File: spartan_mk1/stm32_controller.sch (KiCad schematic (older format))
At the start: 24 parts, among them SW1 SW_SPST, U4 STM32F405RGTx, Y1 X322516MLB4SI

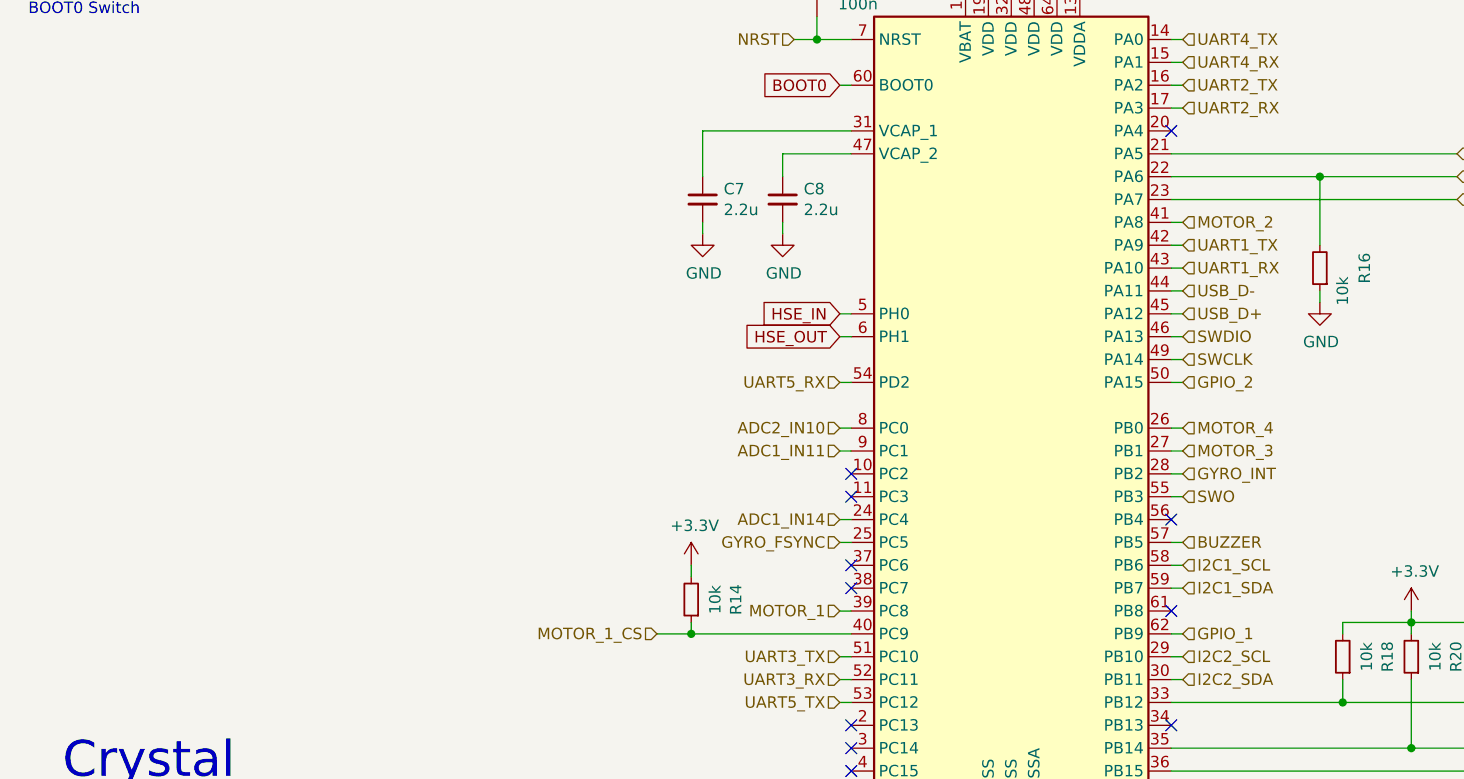
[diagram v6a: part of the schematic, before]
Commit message: Routing complete. Labels complete
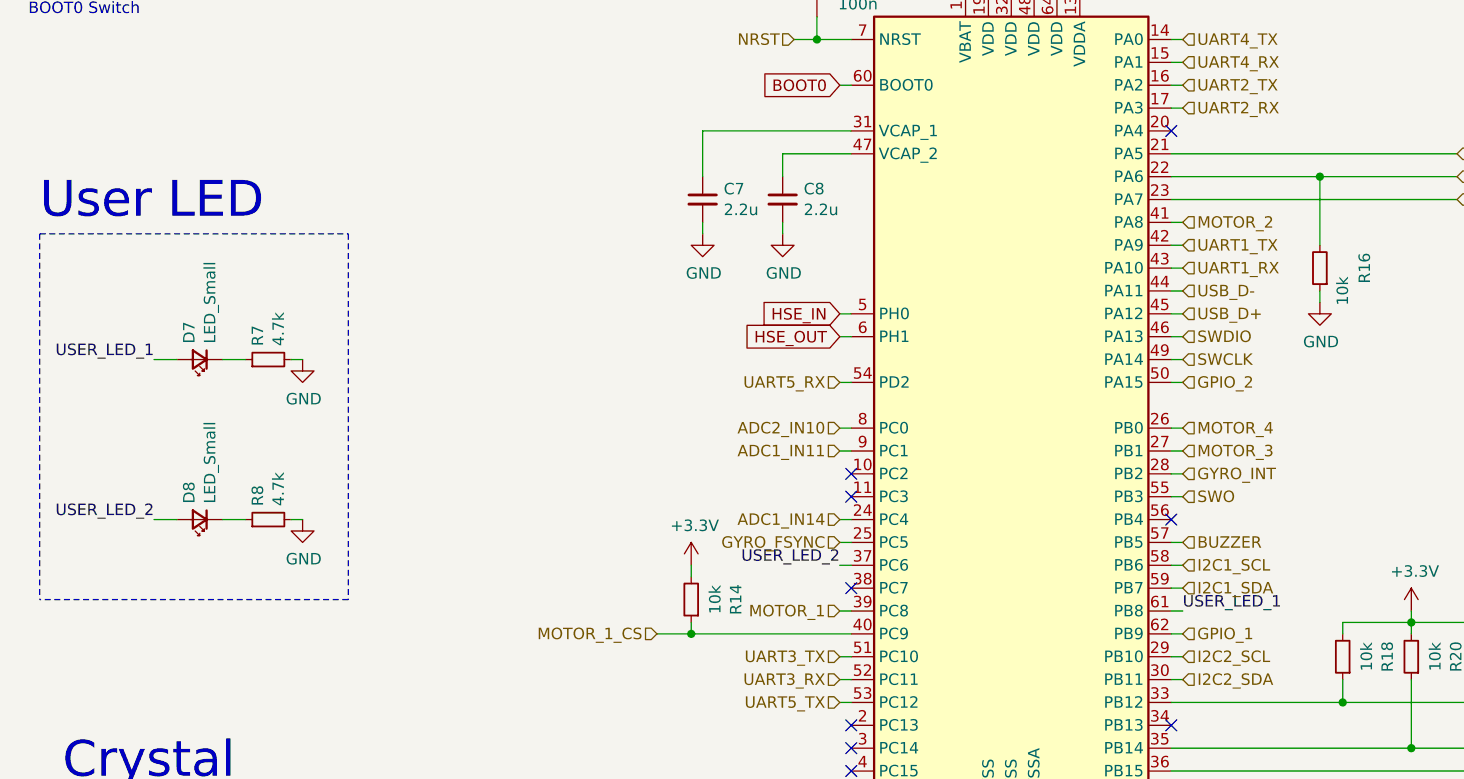
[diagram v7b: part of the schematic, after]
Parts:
- added D7, D8: LED_Small, LED_SMD:LED_0603_1608Metric, symbol Device:LED_Small
- added R7, R8: 4.7k, Resistor_SMD:R_0402_1005Metric, symbol Device:R_Small
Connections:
- net GND: now also R7.2, R8.2
- net USER_LED_2: now reaches U4.37 (PC6)
- net USER_LED_2: now also D8.2 (A)
- net USER_LED_1: now reaches U4.61 (PB8)
- net USER_LED_1: now also D7.2 (A)
- new net: D7.1 (K), R7.1
- new net: D8.1 (K), R8.1
- no-connect marks 11 -> 9
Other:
- note added: "User LED"
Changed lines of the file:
@@
 Wire Wire Line
 	6000 4200 5950 4200
-$Comp
-L MCU_ST_STM32F4:STM32F405RGTx U4
-U 1 1 5F7B167F
-P 5250 4300
-F 0 "U4" H 4750 6100 50  0000 C CNN
-F 1 "STM32F405RGTx" H 5750 2550 50  0000 C CNN
-F 2 "Package_QFP:LQFP-64_10x10mm_P0.5mm" H 4650 2600 50  0001 R CNN
-F 3 "http://www.st.com/st-web-ui/static/active/en/resource/technical/document/datasheet/DM00037051.pdf" H 5250 4300 50  0001 C CNN
-	1    5250 4300
-	1    0    0    -1
-$EndComp
 NoConn ~ 4550 5700
 NoConn ~ 4550 5800
@@
 Text HLabel 4300 2700 0    50   Input ~ 0
 NRST
-NoConn ~ 4550 5000
 NoConn ~ 4550 5100
 Text HLabel 4500 4200 0    50   Input ~ 0
@@
 	5350 6150 5250 6150
 Connection ~ 5250 6150
-NoConn ~ 5950 5200
 NoConn ~ 5950 5700
 NoConn ~ 4550 4700
@@
 Wire Wire Line
 	4400 2700 4550 2700
+Text Notes 1000 3500 0    157  ~ 0
+User LED
+$Comp
+L Device:LED_Small D?
+U 1 1 5FA6EB8E
+P 1700 4100
+AR Path="/5F78701C/5FA6EB8E" Ref="D?"  Part="1"
+AR Path="/5F79A745/5FA6EB8E" Ref="D?"  Part="1"
+AR Path="/5F6A010E/5FA6EB8E" Ref="D7"  Part="1"
+F 0 "D7" V 1746 4030 50  0000 R CNN
+F 1 "LED_Small" V 1655 4030 50  0000 R CNN
+F 2 "LED_SMD:LED_0603_1608Metric" V 1700 4100 50  0001 C CNN
+F 3 "~" V 1700 4100 50  0001 C CNN
+	1    1700 4100
+	-1   0    0    1
+$EndComp
+$Comp
+L Device:R_Small R?
+U 1 1 5FA6EB94
+P 2000 4100
+AR Path="/5F78701C/5FA6EB94" Ref="R?"  Part="1"
+AR Path="/5F79A745/5FA6EB94" Ref="R?"  Part="1"
+AR Path="/5F6A010E/5FA6EB94" Ref="R7"  Part="1"
+F 0 "R7" H 2059 4146 50  0000 L CNN
+F 1 "4.7k" H 2059 4055 50  0000 L CNN
+F 2 "Resistor_SMD:R_0402_1005Metric" H 2000 4100 50  0001 C CNN
+F 3 "~" H 2000 4100 50  0001 C CNN
+	1    2000 4100
+	0    -1   -1   0
+$EndComp
+$Comp
+L power:GND #PWR?
+U 1 1 5FA6EB9C
+P 2150 4100
+AR Path="/5F78701C/5FA6EB9C" Ref="#PWR?"  Part="1"
+AR Path="/5F79A745/5FA6EB9C" Ref="#PWR?"  Part="1"
+AR Path="/5F6A010E/5FA6EB9C" Ref="#PWR012"  Part="1"
+F 0 "#PWR012" H 2150 3850 50  0001 C CNN
+F 1 "GND" H 2155 3927 50  0000 C CNN
+F 2 "" H 2150 4100 50  0001 C CNN
+F 3 "" H 2150 4100 50  0001 C CNN
+	1    2150 4100
+	1    0    0    -1
+$EndComp
+Wire Wire Line
+	2150 4100 2100 4100
+Text Label 1500 4100 2    50   ~ 0
+USER_LED_1
+Wire Wire Line
+	1900 4100 1800 4100
+Wire Wire Line
+	1500 4100 1600 4100
+Wire Notes Line
+	1000 3550 2350 3550
+Wire Wire Line
+	5950 5200 6000 5200
+Text Label 6000 5200 0    50   ~ 0
+USER_LED_1
+$Comp
+L Device:LED_Small D?
+U 1 1 5FAC4CB8
+P 1700 4800
+AR Path="/5F78701C/5FAC4CB8" Ref="D?"  Part="1"
+AR Path="/5F79A745/5FAC4CB8" Ref="D?"  Part="1"
+AR Path="/5F6A010E/5FAC4CB8" Ref="D8"  Part="1"
+F 0 "D8" V 1746 4730 50  0000 R CNN
+F 1 "LED_Small" V 1655 4730 50  0000 R CNN
+F 2 "LED_SMD:LED_0603_1608Metric" V 1700 4800 50  0001 C CNN
+F 3 "~" V 1700 4800 50  0001 C CNN
+	1    1700 4800
+	-1   0    0    1
+$EndComp
+$Comp
+L Device:R_Small R?
+U 1 1 5FAC4CBE
+P 2000 4800
+AR Path="/5F78701C/5FAC4CBE" Ref="R?"  Part="1"
+AR Path="/5F79A745/5FAC4CBE" Ref="R?"  Part="1"
+AR Path="/5F6A010E/5FAC4CBE" Ref="R8"  Part="1"
+F 0 "R8" H 2059 4846 50  0000 L CNN
+F 1 "4.7k" H 2059 4755 50  0000 L CNN
+F 2 "Resistor_SMD:R_0402_1005Metric" H 2000 4800 50  0001 C CNN
+F 3 "~" H 2000 4800 50  0001 C CNN
+	1    2000 4800
+	0    -1   -1   0
+$EndComp
+$Comp
+L power:GND #PWR?
+U 1 1 5FAC4CC4
+P 2150 4800
+AR Path="/5F78701C/5FAC4CC4" Ref="#PWR?"  Part="1"
+AR Path="/5F79A745/5FAC4CC4" Ref="#PWR?"  Part="1"
+AR Path="/5F6A010E/5FAC4CC4" Ref="#PWR013"  Part="1"
+F 0 "#PWR013" H 2150 4550 50  0001 C CNN
+F 1 "GND" H 2155 4627 50  0000 C CNN
+F 2 "" H 2150 4800 50  0001 C CNN
+F 3 "" H 2150 4800 50  0001 C CNN
+	1    2150 4800
+	1    0    0    -1
+$EndComp
+Wire Wire Line
+	2150 4800 2100 4800
+Text Label 1500 4800 2    50   ~ 0
+USER_LED_2
+Wire Wire Line
+	1900 4800 1800 4800
+Wire Wire Line
+	1500 4800 1600 4800
+Wire Notes Line
+	2350 5150 1000 5150
+Wire Notes Line
+	1000 3550 1000 5150
+Wire Notes Line
+	2350 3550 2350 5150
+Text Label 4500 5000 2    50   ~ 0
+USER_LED_2
+Wire Wire Line
+	4550 5000 4500 5000
+$Comp
+L MCU_ST_STM32F4:STM32F405RGTx U4
+U 1 1 5F7B167F
+P 5250 4300
+F 0 "U4" H 4750 6100 50  0000 C CNN
+F 1 "STM32F405RGTx" H 5750 2550 50  0000 C CNN
+F 2 "Package_QFP:LQFP-64_10x10mm_P0.5mm" H 4650 2600 50  0001 R CNN
+F 3 "http://www.st.com/st-web-ui/static/active/en/resource/technical/document/datasheet/DM00037051.pdf" H 5250 4300 50  0001 C CNN
+	1    5250 4300
+	1    0    0    -1
+$EndComp
 $EndSCHEMATC

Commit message: Generated gerber files. Positions and BOM assemly files generated
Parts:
- C10, C12, C14, C15, C16, C17: LCSC (none) -> C1525; LCSC Part # (none) -> C1525
- C11: LCSC (none) -> C52923; LCSC Part # (none) -> C52923
- C13: LCSC (none) -> C15195; LCSC Part # (none) -> C15195
- C5, C6: LCSC (none) -> C1547; LCSC Part # (none) -> C1547
- C7, C8: footprint Capacitor_SMD:C_0402_1005Metric -> Capacitor_SMD:C_0603_1608Metric; LCSC (none) -> C12530; LCSC Part # (none) -> C12530
- C9: LCSC (none) -> C23733; LCSC Part # (none) -> C23733
- D7: value LED_Small -> LED_GREEN; LCSC (none) -> C205443; LCSC Part # (none) -> C205443
- D8: value LED_Small -> LED_BLUE; LCSC (none) -> C72041; LCSC Part # (none) -> C72041
- L1: LCSC (none) -> C18830; LCSC Part # (none) -> C18830
- R12, R14, R16, R18, R20, R21: LCSC (none) -> C25744; LCSC Part # (none) -> C25744
- R13: footprint Resistor_SMD:R_0603_1608Metric -> Resistor_SMD:R_0402_1005Metric; LCSC (none) -> C25118; LCSC Part # (none) -> C25118
- R7, R8: LCSC (none) -> C25900; LCSC Part # (none) -> C25900
- U4: LCSC (none) -> C15742; LCSC Part # (none) -> C15742
- Y1: LCSC (none) -> C13738; LCSC Part # (none) -> C13738
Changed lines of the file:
@@
 F 0 "C8" H 4342 3446 50  0000 L CNN
 F 1 "2.2u" H 4342 3355 50  0000 L CNN
-F 2 "Capacitor_SMD:C_0402_1005Metric" H 4250 3400 50  0001 C CNN
+F 2 "Capacitor_SMD:C_0603_1608Metric" H 4250 3400 50  0001 C CNN
 F 3 "~" H 4250 3400 50  0001 C CNN
+F 4 "C12530" H 4250 3400 50  0001 C CNN "LCSC Part #"
+F 5 "C12530" H 4250 3400 50  0001 C CNN "LCSC"
 	1    4250 3400
 	1    0    0    -1
@@
 F 0 "C7" H 3992 3446 50  0000 L CNN
 F 1 "2.2u" H 3992 3355 50  0000 L CNN
-F 2 "Capacitor_SMD:C_0402_1005Metric" H 3900 3400 50  0001 C CNN
+F 2 "Capacitor_SMD:C_0603_1608Metric" H 3900 3400 50  0001 C CNN
 F 3 "~" H 3900 3400 50  0001 C CNN
+F 4 "C12530" H 3900 3400 50  0001 C CNN "LCSC Part #"
+F 5 "C12530" H 3900 3400 50  0001 C CNN "LCSC"
 	1    3900 3400
 	1    0    0    -1
@@
 F 2 "Resistor_SMD:R_0402_1005Metric" H 1750 1750 50  0001 C CNN
 F 3 "~" H 1750 1750 50  0001 C CNN
+F 4 "C25744" H 1750 1750 50  0001 C CNN "LCSC Part #"
+F 5 "C25744" H 1750 1750 50  0001 C CNN "LCSC"
 	1    1750 1750
 	0    1    1    0
@@
 F 2 "Capacitor_SMD:C_0402_1005Metric" H 8800 1500 50  0001 C CNN
 F 3 "~" H 8800 1500 50  0001 C CNN
+F 4 "C23733" H 8800 1500 50  0001 C CNN "LCSC Part #"
+F 5 "C23733" H 8800 1500 50  0001 C CNN "LCSC"
 	1    8800 1500
 	1    0    0    -1
@@
 F 2 "Capacitor_SMD:C_0402_1005Metric" H 9150 1500 50  0001 C CNN
 F 3 "~" H 9150 1500 50  0001 C CNN
+F 4 "C1525" H 9150 1500 50  0001 C CNN "LCSC Part #"
+F 5 "C1525" H 9150 1500 50  0001 C CNN "LCSC"
 	1    9150 1500
 	1    0    0    -1
@@
 F 2 "Capacitor_SMD:C_0402_1005Metric" H 9500 1500 50  0001 C CNN
 F 3 "~" H 9500 1500 50  0001 C CNN
+F 4 "C1525" H 9500 1500 50  0001 C CNN "LCSC Part #"
+F 5 "C1525" H 9500 1500 50  0001 C CNN "LCSC"
 	1    9500 1500
 	1    0    0    -1
@@
 F 2 "Capacitor_SMD:C_0402_1005Metric" H 9850 1500 50  0001 C CNN
 F 3 "~" H 9850 1500 50  0001 C CNN
+F 4 "C1525" H 9850 1500 50  0001 C CNN "LCSC Part #"
+F 5 "C1525" H 9850 1500 50  0001 C CNN "LCSC"
 	1    9850 1500
 	1    0    0    -1
@@
 F 2 "Capacitor_SMD:C_0402_1005Metric" H 10200 1500 50  0001 C CNN
 F 3 "~" H 10200 1500 50  0001 C CNN
+F 4 "C1525" H 10200 1500 50  0001 C CNN "LCSC Part #"
+F 5 "C1525" H 10200 1500 50  0001 C CNN "LCSC"
 	1    10200 1500
 	1    0    0    -1
@@
 F 2 "Capacitor_SMD:C_0402_1005Metric" H 10550 1500 50  0001 C CNN
 F 3 "~" H 10550 1500 50  0001 C CNN
+F 4 "C1525" H 10550 1500 50  0001 C CNN "LCSC Part #"
+F 5 "C1525" H 10550 1500 50  0001 C CNN "LCSC"
 	1    10550 1500
 	1    0    0    -1
@@
 F 2 "Capacitor_SMD:C_0402_1005Metric" H 9300 2650 50  0001 C CNN
 F 3 "~" H 9300 2650 50  0001 C CNN
+F 4 "C52923" H 9300 2650 50  0001 C CNN "LCSC Part #"
+F 5 "C52923" H 9300 2650 50  0001 C CNN "LCSC"
 	1    9300 2650
 	1    0    0    -1
@@
 F 2 "Capacitor_SMD:C_0402_1005Metric" H 9600 2650 50  0001 C CNN
 F 3 "~" H 9600 2650 50  0001 C CNN
+F 4 "C15195" H 9600 2650 50  0001 C CNN "LCSC Part #"
+F 5 "C15195" H 9600 2650 50  0001 C CNN "LCSC"
 	1    9600 2650
 	1    0    0    -1
@@
 F 2 "Inductor_SMD:L_0402_1005Metric" H 9050 2550 50  0001 C CNN
 F 3 "~" H 9050 2550 50  0001 C CNN
+F 4 "C18830" H 9050 2550 50  0001 C CNN "LCSC Part #"
+F 5 "C18830" H 9050 2550 50  0001 C CNN "LCSC"
 	1    9050 2550
 	0    -1   -1   0
@@
 F 2 "Crystal:Crystal_SMD_3225-4Pin_3.2x2.5mm" H 1900 6500 50  0001 C CNN
 F 3 "~" H 1900 6500 50  0001 C CNN
+F 4 "C13738" H 1900 6500 50  0001 C CNN "LCSC Part #"
+F 5 "C13738" H 1900 6500 50  0001 C CNN "LCSC"
 	1    1900 6500
 	1    0    0    -1
@@
 F 2 "Capacitor_SMD:C_0402_1005Metric" H 2150 6700 50  0001 C CNN
 F 3 "~" H 2150 6700 50  0001 C CNN
+F 4 "C1547" H 2150 6700 50  0001 C CNN "LCSC Part #"
+F 5 "C1547" H 2150 6700 50  0001 C CNN "LCSC"
 	1    2150 6700
 	1    0    0    -1
@@
 F 2 "Capacitor_SMD:C_0402_1005Metric" H 1650 6700 50  0001 C CNN
 F 3 "~" H 1650 6700 50  0001 C CNN
+F 4 "C1547" H 1650 6700 50  0001 C CNN "LCSC Part #"
+F 5 "C1547" H 1650 6700 50  0001 C CNN "LCSC"
 	1    1650 6700
 	1    0    0    -1
@@
 F 0 "R13" H 2209 6396 50  0000 L CNN
 F 1 "47" H 2209 6305 50  0000 L CNN
-F 2 "Resistor_SMD:R_0603_1608Metric" H 2150 6350 50  0001 C CNN
+F 2 "Resistor_SMD:R_0402_1005Metric" H 2150 6350 50  0001 C CNN
 F 3 "~" H 2150 6350 50  0001 C CNN
+F 4 "C25118" H 2150 6350 50  0001 C CNN "LCSC Part #"
+F 5 "C25118" H 2150 6350 50  0001 C CNN "LCSC"
 	1    2150 6350
 	1    0    0    -1
@@
 F 2 "Resistor_SMD:R_0402_1005Metric" H 6700 5400 50  0001 C CNN
 F 3 "~" H 6700 5400 50  0001 C CNN
+F 4 "C25744" H 6700 5400 50  0001 C CNN "LCSC Part #"
+F 5 "C25744" H 6700 5400 50  0001 C CNN "LCSC"
 	1    6700 5400
 	-1   0    0    1
@@
 F 2 "Resistor_SMD:R_0402_1005Metric" H 7000 5400 50  0001 C CNN
 F 3 "~" H 7000 5400 50  0001 C CNN
+F 4 "C25744" H 7000 5400 50  0001 C CNN "LCSC Part #"
+F 5 "C25744" H 7000 5400 50  0001 C CNN "LCSC"
 	1    7000 5400
 	-1   0    0    1
@@
 F 2 "Resistor_SMD:R_0402_1005Metric" H 7300 5400 50  0001 C CNN
 F 3 "~" H 7300 5400 50  0001 C CNN
+F 4 "C25744" H 7300 5400 50  0001 C CNN "LCSC Part #"
+F 5 "C25744" H 7300 5400 50  0001 C CNN "LCSC"
 	1    7300 5400
 	-1   0    0    1
@@
 F 2 "Resistor_SMD:R_0402_1005Metric" H 3850 5150 50  0001 C CNN
 F 3 "~" H 3850 5150 50  0001 C CNN
+F 4 "C25744" H 3850 5150 50  0001 C CNN "LCSC Part #"
+F 5 "C25744" H 3850 5150 50  0001 C CNN "LCSC"
 	1    3850 5150
 	-1   0    0    1
@@
 F 2 "Resistor_SMD:R_0402_1005Metric" H 6600 3700 50  0001 C CNN
 F 3 "~" H 6600 3700 50  0001 C CNN
+F 4 "C25744" H 6600 3700 50  0001 C CNN "LCSC Part #"
+F 5 "C25744" H 6600 3700 50  0001 C CNN "LCSC"
 	1    6600 3700
 	-1   0    0    1
@@
 F 2 "Capacitor_SMD:C_0402_1005Metric" H 4400 2500 50  0001 C CNN
 F 3 "~" H 4400 2500 50  0001 C CNN
+F 4 "C1525" H 4400 2500 50  0001 C CNN "LCSC Part #"
+F 5 "C1525" H 4400 2500 50  0001 C CNN "LCSC"
 	1    4400 2500
 	1    0    0    -1
@@
 AR Path="/5F6A010E/5FA6EB8E" Ref="D7"  Part="1"
 F 0 "D7" V 1746 4030 50  0000 R CNN
-F 1 "LED_Small" V 1655 4030 50  0000 R CNN
+F 1 "LED_GREEN" V 1655 4030 50  0000 R CNN
 F 2 "LED_SMD:LED_0603_1608Metric" V 1700 4100 50  0001 C CNN
 F 3 "~" V 1700 4100 50  0001 C CNN
+F 4 "C205443" H 1700 4100 50  0001 C CNN "LCSC Part #"
+F 5 "C205443" H 1700 4100 50  0001 C CNN "LCSC"
 	1    1700 4100
 	-1   0    0    1
@@
 F 2 "Resistor_SMD:R_0402_1005Metric" H 2000 4100 50  0001 C CNN
 F 3 "~" H 2000 4100 50  0001 C CNN
+F 4 "C25900" H 2000 4100 50  0001 C CNN "LCSC Part #"
+F 5 "C25900" H 2000 4100 50  0001 C CNN "LCSC"
 	1    2000 4100
 	0    -1   -1   0
@@
 AR Path="/5F6A010E/5FAC4CB8" Ref="D8"  Part="1"
 F 0 "D8" V 1746 4730 50  0000 R CNN
-F 1 "LED_Small" V 1655 4730 50  0000 R CNN
+F 1 "LED_BLUE" V 1655 4730 50  0000 R CNN
 F 2 "LED_SMD:LED_0603_1608Metric" V 1700 4800 50  0001 C CNN
 F 3 "~" V 1700 4800 50  0001 C CNN
+F 4 "C72041" H 1700 4800 50  0001 C CNN "LCSC Part #"
+F 5 "C72041" H 1700 4800 50  0001 C CNN "LCSC"
 	1    1700 4800
 	-1   0    0    1
@@
 F 2 "Resistor_SMD:R_0402_1005Metric" H 2000 4800 50  0001 C CNN
 F 3 "~" H 2000 4800 50  0001 C CNN
+F 4 "C25900" H 2000 4800 50  0001 C CNN "LCSC Part #"
+F 5 "C25900" H 2000 4800 50  0001 C CNN "LCSC"
 	1    2000 4800
 	0    -1   -1   0
@@
 F 2 "Package_QFP:LQFP-64_10x10mm_P0.5mm" H 4650 2600 50  0001 R CNN
 F 3 "http://www.st.com/st-web-ui/static/active/en/resource/technical/document/datasheet/DM00037051.pdf" H 5250 4300 50  0001 C CNN
+F 4 "C15742" H 5250 4300 50  0001 C CNN "LCSC Part #"
+F 5 "C15742" H 5250 4300 50  0001 C CNN "LCSC"
 	1    5250 4300
 	1    0    0    -1
